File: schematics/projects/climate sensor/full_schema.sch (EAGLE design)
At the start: 46 parts, among them J1 J2, J10 KF301-5.0, J11 J4_FS_2, J2 J2, J3 J2, J4 J2, J4_FS_1 KF301-5.0, J5 WAY AMP 4PIN, J6 WAY AMP 4PIN, J7 KF301-5.0, J8 KF301-5.0, J9 KF301-5.0, Q1 2N3904, Q2 2N3904, Q3 2N3904, Q4 2N3904, Q5 2N3904, Q6 2N3904, U1 BME280, U2 PMS7003, U3 ESP32 DEVKIT WROOM-32D

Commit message: rename elements, optimize board
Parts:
- removed GY_SGP30_1: GY-SGP30, my_devices:GY-SGP30
- removed J4_FS_1: KF301-5.0, my_devices:J2
- added J12: J4_FS_2, my_devices:J2
- added U5: BME280, my_devices:BME280
- J1, J2: value J2 -> WAY AMP 4PIN; device my_devices:J2 -> my_devices:J4
- J10, J8, J9: value KF301-5.0 -> J2
- J11: value J4_FS_2 -> J2
- J3, J4: value J2 -> KF301-5.0
- J5, J6: value WAY AMP 4PIN -> KF301-5.0; device my_devices:J4 -> my_devices:J2
- R1: value 10K -> 600
- R11: value 30 -> 600
- R12: value 100 -> 600
- R14: value 10K -> 100
- R7: value 600 -> 30
- R8, R9: value 600 -> 10K
- U1: value BME280 -> GY-SGP30; device my_devices:BME280 -> my_devices:GY-SGP30
- U2: value PMS7003 -> ESP32 DEVKIT WROOM-32D; device my_devices:PMS7003 -> my_devices:ESP32
- U3: value ESP32 DEVKIT WROOM-32D -> PMS7003; device my_devices:ESP32 -> my_devices:PMS7003
- renumbered U$10 to FAN1, U$11 to U6, U$4 to U4, U$6 to D2, U$7 to TSW1, U$8 to ANM1, U$9 to ACDC1
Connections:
- removed net N$23 (its old number): Q3.B, R6.P$2
- new net N$27: Q3.B, R10.P$2
- net +5V: now also J10.PIN_2, J5.PIN_2, Q4.C, Q5.C, Q6.C, R1.P$2, R14.P$1, R4.P$2; no longer J3.PIN_2, J7.PIN_2, Q1.C, Q2.C, Q3.C, R10.P$2, R12.P$1, R9.P$2
- net 220V_OUT_L: now also J9.PIN_1; no longer J1.PIN_1
- net 220V_OUT_N: now also J9.PIN_2; no longer J1.PIN_2
- net 3V3: now also R2.P$2, R5.P$2, R7.P$1, R8.P$1, R9.P$1, U1.VIN; no longer GY_SGP30_1.VIN, R1.P$1, R11.P$1, R14.P$1, R7.P$2, R8.P$2
- net 5V: now also U2.5V; no longer U3.5V
- net ACDC_OUT_5V: now also J8.PIN_1; no longer J2.PIN_1
- net GND: now also J1.PIN_4, J10.PIN_1, J12.PIN_2, J5.PIN_1, J7.PIN_2, Q1.E, Q2.E, Q3.E, U5.GND; no longer GY_SGP30_1.GND, J11.PIN_2, J3.PIN_1, J4_FS_1.PIN_2, J6.PIN_4, J7.PIN_1, Q4.E, Q5.E, Q6.E
- net GPIO_AN_A: now also R3.P$2, U2.IO34; no longer R2.P$2, U3.IO34
- net GPIO_AN_B: now also R6.P$2, U2.IO35; no longer R3.P$2, U3.IO35
- net GPIO_IR: now also R10.P$1, U2.IO2; no longer R13.P$1, U3.IO2
- net GPIO_RGB_B: now also R11.P$1, U2.IO27; no longer R4.P$1, U3.IO27
- net GPIO_RGB_G: now also R12.P$1, U2.IO26; no longer R5.P$1, U3.IO26
- net GPIO_RGB_R: now also R13.P$1, U2.IO25; no longer R6.P$1, U3.IO25
- net GPIO_TS: now also U2.IO4; no longer U3.IO4
- net I2C_SCL: now also U2.IO23, U5.SCL; no longer GY_SGP30_1.SCL, U3.IO23
- net I2C_SDA: now also U2.IO21, U5.SDA; no longer GY_SGP30_1.SDA, U3.IO21
- net N$1: now also Q4.E; no longer Q1.E
- net N$10: now also J7.PIN_1; no longer J4_FS_1.PIN_1
- net N$11: now also J12.PIN_1, U2.IO32; no longer J11.PIN_1, U3.IO32
- net N$12: now also J1.PIN_3; no longer J6.PIN_3
- net N$13: now also J1.PIN_2; no longer J6.PIN_2
- net N$14: now also J1.PIN_1; no longer J6.PIN_1
- net N$15: now also J11.PIN_1; no longer J4.PIN_1
- net N$16: now also J11.PIN_2; no longer J4.PIN_2
- net N$17: now also J2.PIN_1, J3.PIN_2; no longer J5.PIN_1, J9.PIN_2
- net N$18: now also J2.PIN_2, J3.PIN_1; no longer J5.PIN_2, J9.PIN_1
- net N$19: now also J2.PIN_3, J4.PIN_2; no longer J10.PIN_2, J5.PIN_3
- net N$2: now also Q5.E; no longer Q2.E
- net N$20: now also J2.PIN_4, J4.PIN_1; no longer J10.PIN_1, J5.PIN_4
- net N$21: now also Q4.B, R11.P$2; no longer Q1.B, R4.P$2
- net N$22: now also Q5.B, R12.P$2; no longer Q2.B, R5.P$2
- net N$24: now also R7.P$2, U2.3V3; no longer R11.P$2, U3.3V3
- net N$25: now also Q3.C; no longer Q6.C
- net N$26: now also R14.P$2; no longer R12.P$2
- net N$28: now also R9.P$2, U3.SET; no longer R14.P$2, U2.SET
- net N$3: now also Q6.E; no longer Q3.E
- net N$4: now also J6.PIN_1, Q2.B, R4.P$1; no longer J8.PIN_1, Q4.B, R10.P$1
- net N$5: now also J6.PIN_2, Q1.B, R1.P$1; no longer J8.PIN_2, Q5.B, R9.P$1
- net N$6: now also Q1.C, R3.P$1; no longer Q5.C, R7.P$1
- net N$7: now also Q2.C, R5.P$1, R6.P$1; no longer Q4.C, R3.P$1, R8.P$1
- net N$8: now also R8.P$2, U3.RESET; no longer R1.P$2, U2.RESET
- net OUT_GND: now also J8.PIN_2; no longer J2.PIN_2
- net UART_0_RXD: now also U2.RXD0; no longer U3.RXD0
- net UART_0_TXD: now also U2.TXD0; no longer U3.TXD0
- net UART_1_RXD: now also U2.SD2, U3.RXD; no longer U2.RXD, U3.SD2
- net UART_1_TXD: now also U2.SD3, U3.TXD; no longer U2.TXD, U3.SD3
- net VCC: now also U3.VCC, U5.VCC; no longer U1.VCC, U2.VCC
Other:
- moved on the sheet: J10, J11, J3, J4, J7, J8, J9, Q1, Q2, Q3, Q4, Q5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

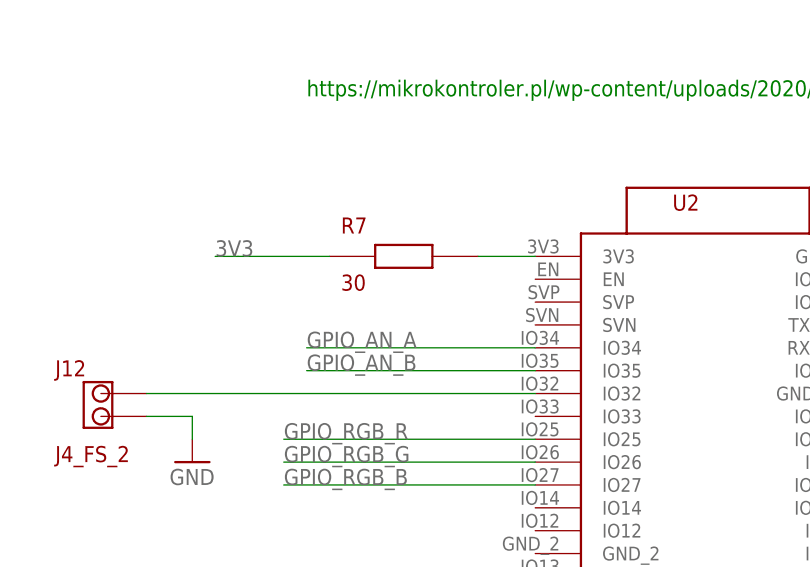
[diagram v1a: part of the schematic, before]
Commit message: SGP30 sensor works now. I2C bus fully tested.
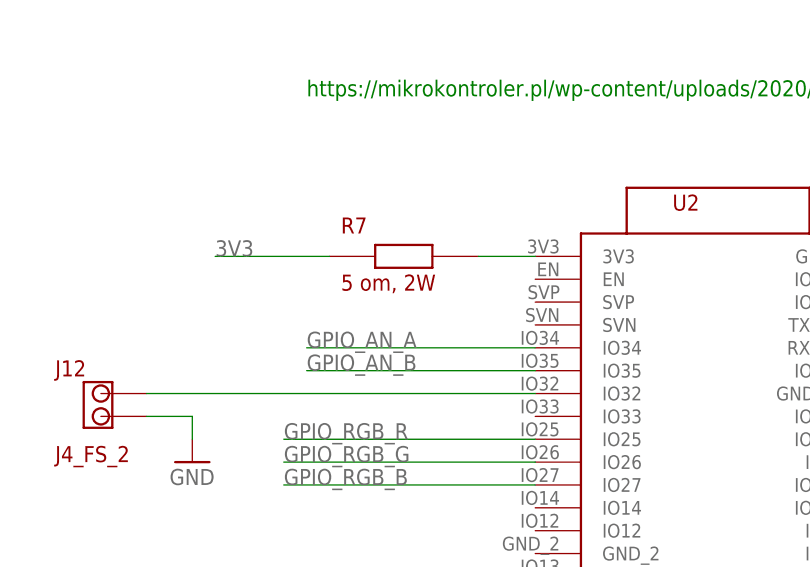
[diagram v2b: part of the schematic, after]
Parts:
- R7: value 30 -> 5 om, 2W
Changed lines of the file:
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@@
 <part name="R1" library="my_devices" deviceset="R" device="" value="600"/>
 <part name="R4" library="my_devices" deviceset="R" device="" value="600"/>
-<part name="R7" library="my_devices" deviceset="R" device="" value="30"/>
+<part name="R7" library="my_devices" deviceset="R" device="" value="5 om, 2W"/>
 <part name="D1" library="my_devices" deviceset="LD" device="" value="IR"/>
 <part name="GND10" library="supply1" library_urn="urn:adsk.eagle:library:371" deviceset="GND" device=""/>

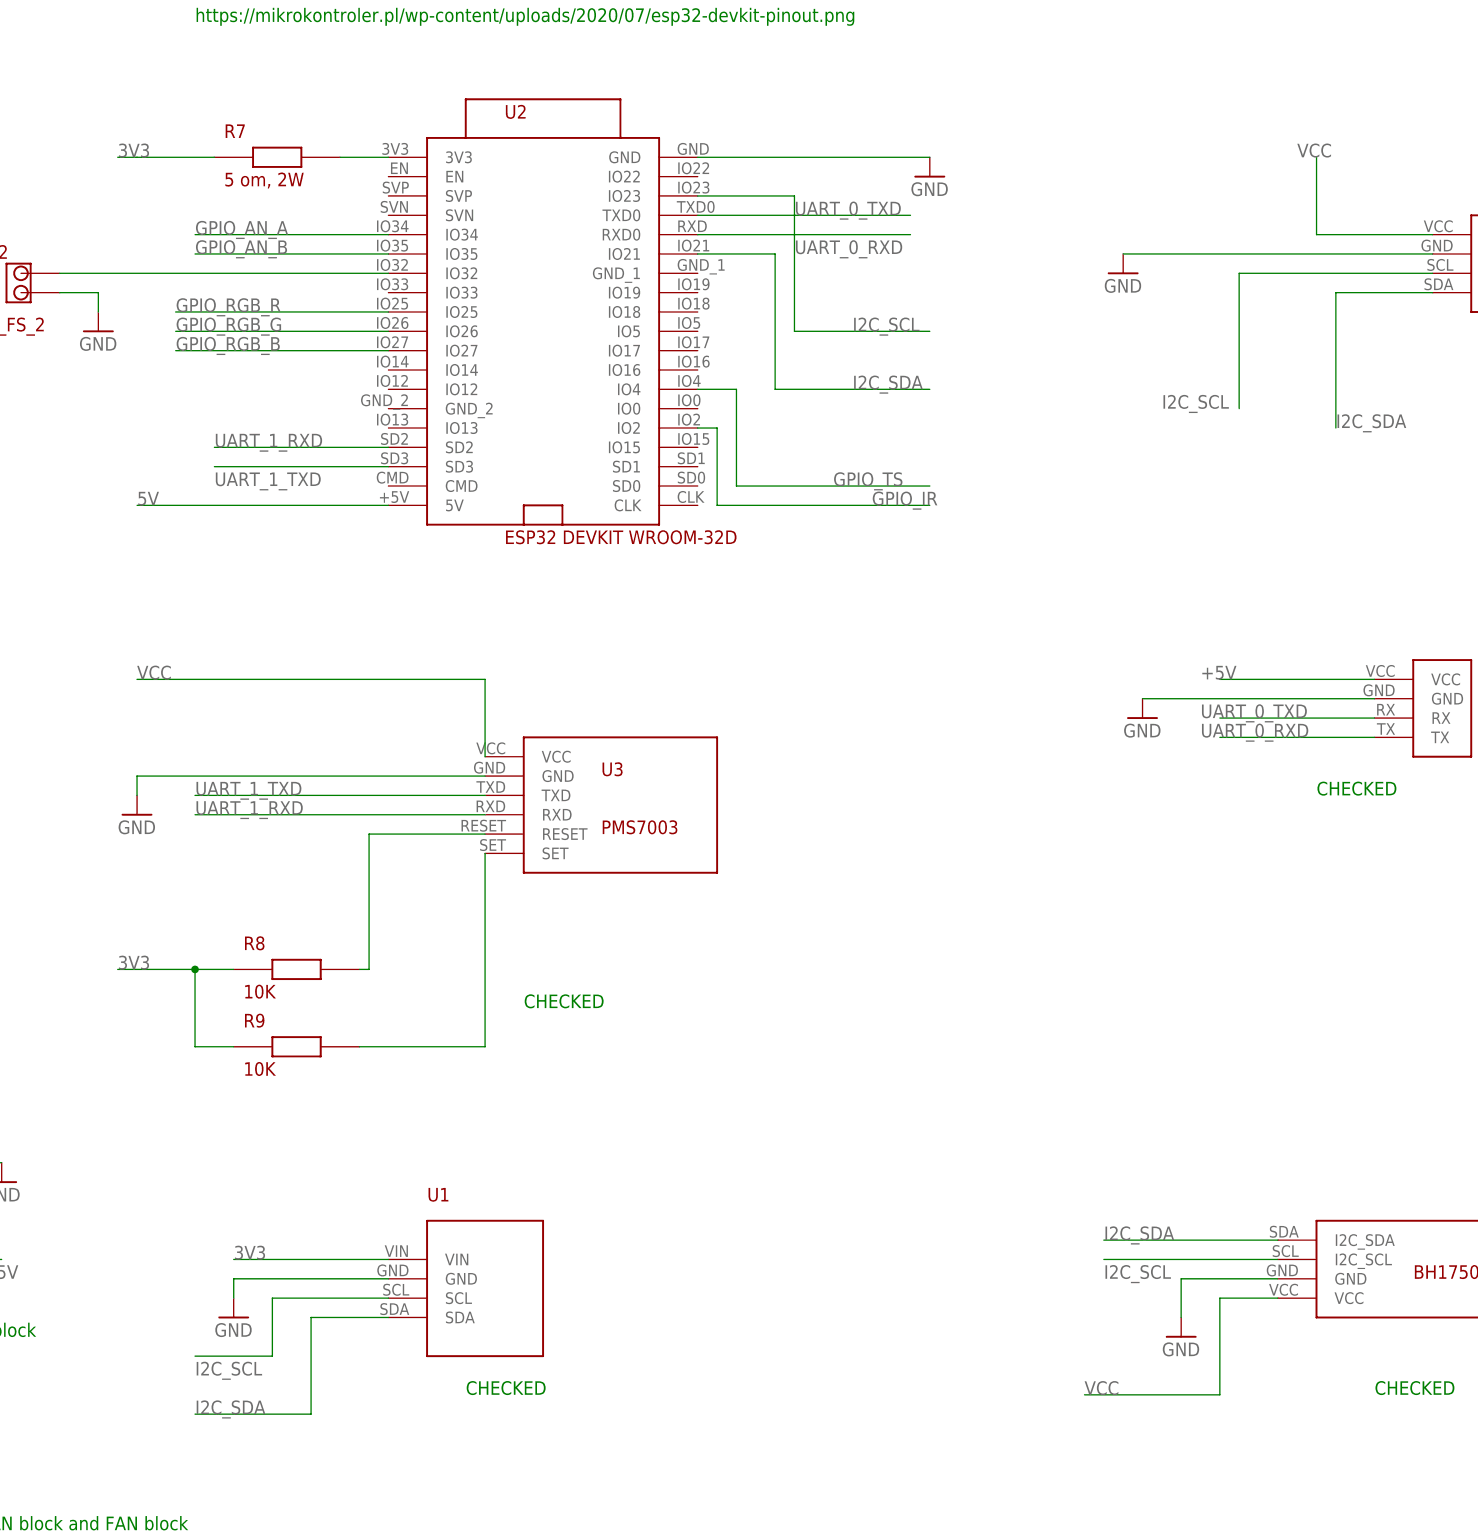
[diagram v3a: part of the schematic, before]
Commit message: Added ability to recalibrate SGP30 sensor (on hot-replace for example to another module)
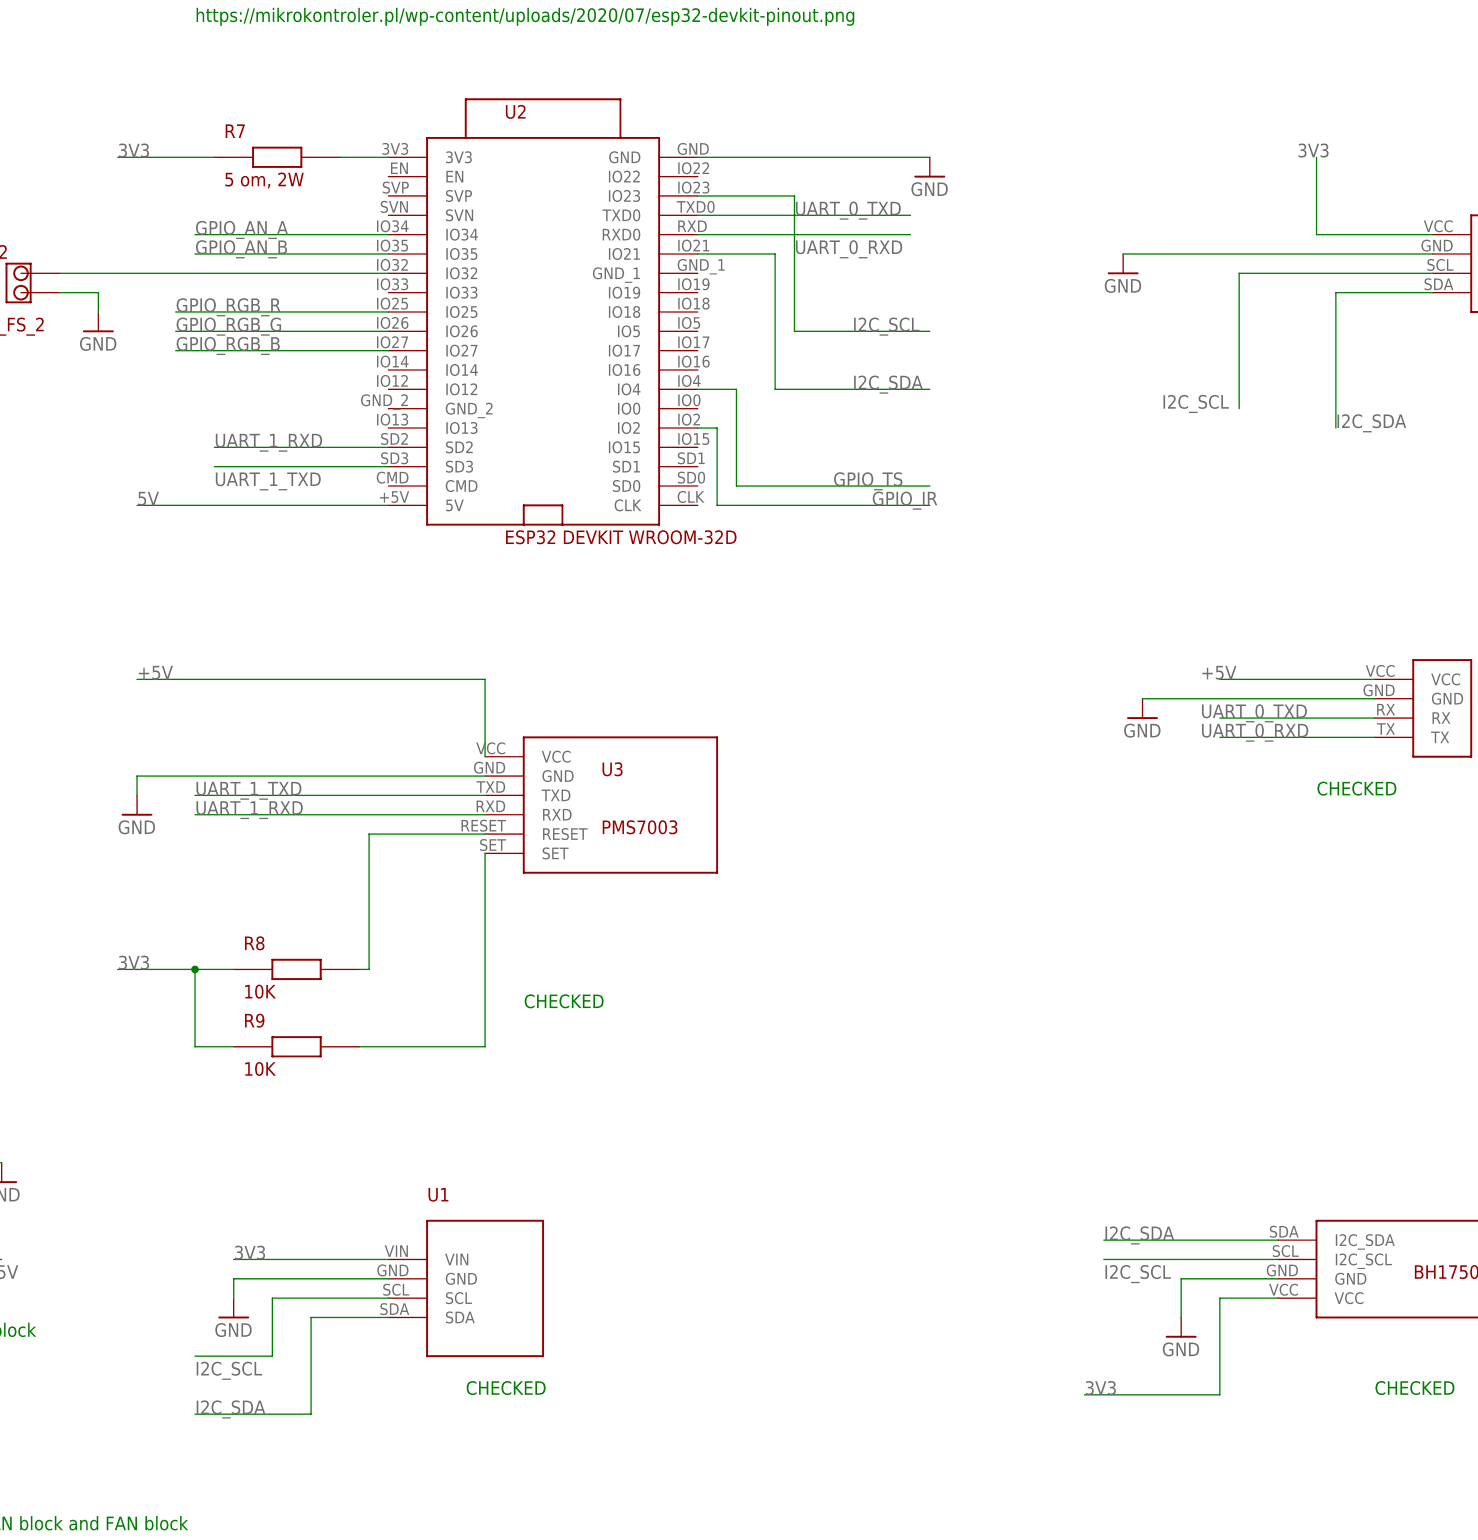
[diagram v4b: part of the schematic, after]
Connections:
- net +5V: now also U3.VCC
- net 3V3: now also U4.VCC, U5.VCC
- net VCC: no longer U3.VCC, U4.VCC, U5.VCC
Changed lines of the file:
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@@
 <label x="213.36" y="27.94" size="1.778" layer="95" grouprefs="RGBLED"/>
+</segment>
+<segment>
+<pinref part="U3" gate="G$1" pin="VCC"/>
+<wire x1="-43.18" y1="25.4" x2="-43.18" y2="35.56" width="0.1524" layer="91" grouprefs="PMS7003"/>
+<wire x1="-43.18" y1="35.56" x2="-88.9" y2="35.56" width="0.1524" layer="91" grouprefs="PMS7003"/>
+<label x="-88.9" y="35.56" size="1.778" layer="95" grouprefs="PMS7003"/>
 </segment>
 </net>
@@
 <wire x1="-91.44" y1="104.14" x2="-88.9" y2="104.14" width="0.1524" layer="91"/>
 <label x="-91.44" y="104.14" size="1.778" layer="95"/>
+</segment>
+<segment>
+<wire x1="81.28" y1="93.98" x2="66.04" y2="93.98" width="0.1524" layer="91" grouprefs="BME_280_TEMP_HUM"/>
+<wire x1="66.04" y1="93.98" x2="66.04" y2="104.14" width="0.1524" layer="91" grouprefs="BME_280_TEMP_HUM"/>
+<label x="63.5" y="104.14" size="1.778" layer="95" grouprefs="BME_280_TEMP_HUM"/>
+<pinref part="U5" gate="G$1" pin="VCC"/>
+</segment>
+<segment>
+<wire x1="60.96" y1="-45.72" x2="53.34" y2="-45.72" width="0.1524" layer="91" grouprefs="BH1750"/>
+<wire x1="53.34" y1="-45.72" x2="53.34" y2="-58.42" width="0.1524" layer="91" grouprefs="BH1750"/>
+<wire x1="53.34" y1="-58.42" x2="35.56" y2="-58.42" width="0.1524" layer="91" grouprefs="BH1750"/>
+<label x="35.56" y="-58.42" size="1.778" layer="95" grouprefs="BH1750"/>
+<pinref part="U4" gate="G$1" pin="VCC"/>
 </segment>
 </net>
@@
 <pinref part="TSW1" gate="G$1" pin="220V_IN_L"/>
 </segment>
-<segment>
-<wire x1="60.96" y1="-45.72" x2="53.34" y2="-45.72" width="0.1524" layer="91" grouprefs="BH1750"/>
-<wire x1="53.34" y1="-45.72" x2="53.34" y2="-58.42" width="0.1524" layer="91" grouprefs="BH1750"/>
-<wire x1="53.34" y1="-58.42" x2="35.56" y2="-58.42" width="0.1524" layer="91" grouprefs="BH1750"/>
-<label x="35.56" y="-58.42" size="1.778" layer="95" grouprefs="BH1750"/>
-<pinref part="U4" gate="G$1" pin="VCC"/>
-</segment>
-<segment>
-<wire x1="81.28" y1="93.98" x2="66.04" y2="93.98" width="0.1524" layer="91" grouprefs="BME_280_TEMP_HUM"/>
-<wire x1="66.04" y1="93.98" x2="66.04" y2="104.14" width="0.1524" layer="91" grouprefs="BME_280_TEMP_HUM"/>
-<label x="63.5" y="104.14" size="1.778" layer="95" grouprefs="BME_280_TEMP_HUM"/>
-<pinref part="U5" gate="G$1" pin="VCC"/>
-</segment>
-<segment>
-<pinref part="U3" gate="G$1" pin="VCC"/>
-<wire x1="-43.18" y1="25.4" x2="-43.18" y2="35.56" width="0.1524" layer="91" grouprefs="PMS7003"/>
-<wire x1="-43.18" y1="35.56" x2="-88.9" y2="35.56" width="0.1524" layer="91" grouprefs="PMS7003"/>
-<label x="-88.9" y="35.56" size="1.778" layer="95" grouprefs="PMS7003"/>
-</segment>
-</net>
+</net>
